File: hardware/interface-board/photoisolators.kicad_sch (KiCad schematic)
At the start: 101 parts, among them IC701 LTV-846S, IC702 LTV-846S, IC703 LTV-846S, IC704 LTV-846S, Q701 BSS138 JI, Q702 BSS138 JI, Q703 BSS138 JI, Q704 BSS138 JI, Q705 BSS138 JI, Q706 BSS138 JI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

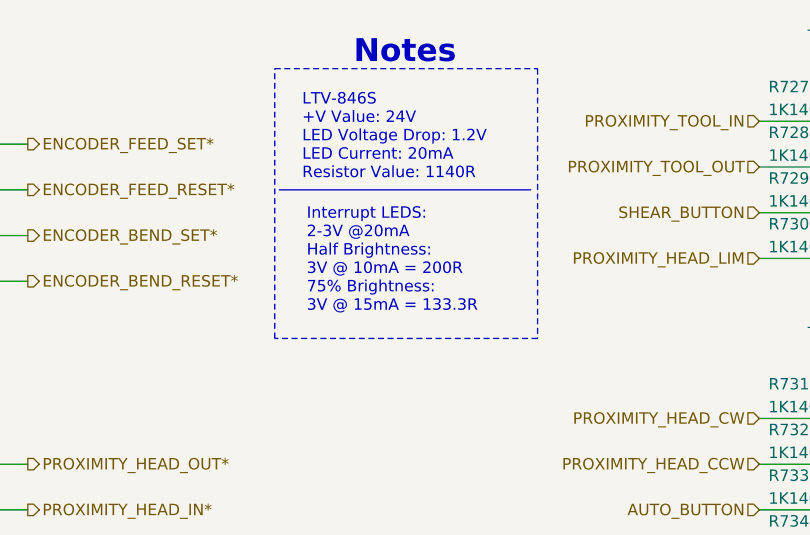
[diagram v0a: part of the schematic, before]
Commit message: X1 Release
Released X1 revision for both the interface board and the input test fixture breakout board.
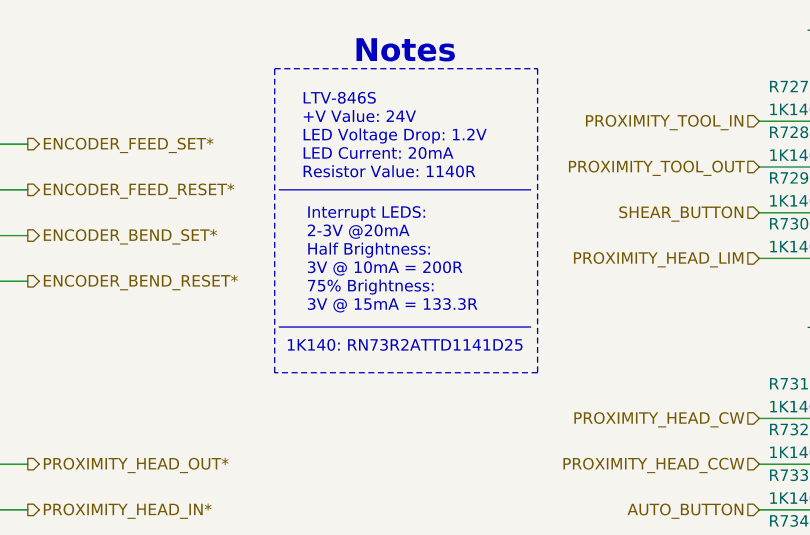
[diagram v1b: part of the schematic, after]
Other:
- note added: "1K140: RN73R2ATTD1141D25"
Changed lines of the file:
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@@
+		)
+	)
+	(polyline
+		(pts
+			(xy 129.54 49.53) (xy 157.48 49.53)
+		)
+		(stroke
+			(width 0)
+			(type default)
 		)
 	)
@@
 	(rectangle
 		(start 129.032 20.828)
-		(end 158.242 50.8)
+		(end 158.242 54.61)
 		(stroke
 			(width 0)
@@
 			)
 		)
+	)
+	(text "1K140: RN73R2ATTD1141D25"
+		(exclude_from_sim no)
+		(at 143.51 51.816 0)
+		(effects
+			(font
+				(size 1.27 1.27)
+			)
+		)
